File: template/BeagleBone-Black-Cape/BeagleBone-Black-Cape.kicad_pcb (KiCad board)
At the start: 2 copper layers, 54.6 x 86.4 mm, 2 parts, among them P8 BeagleBone_Black_Header, P9 BeagleBone_Black_Header

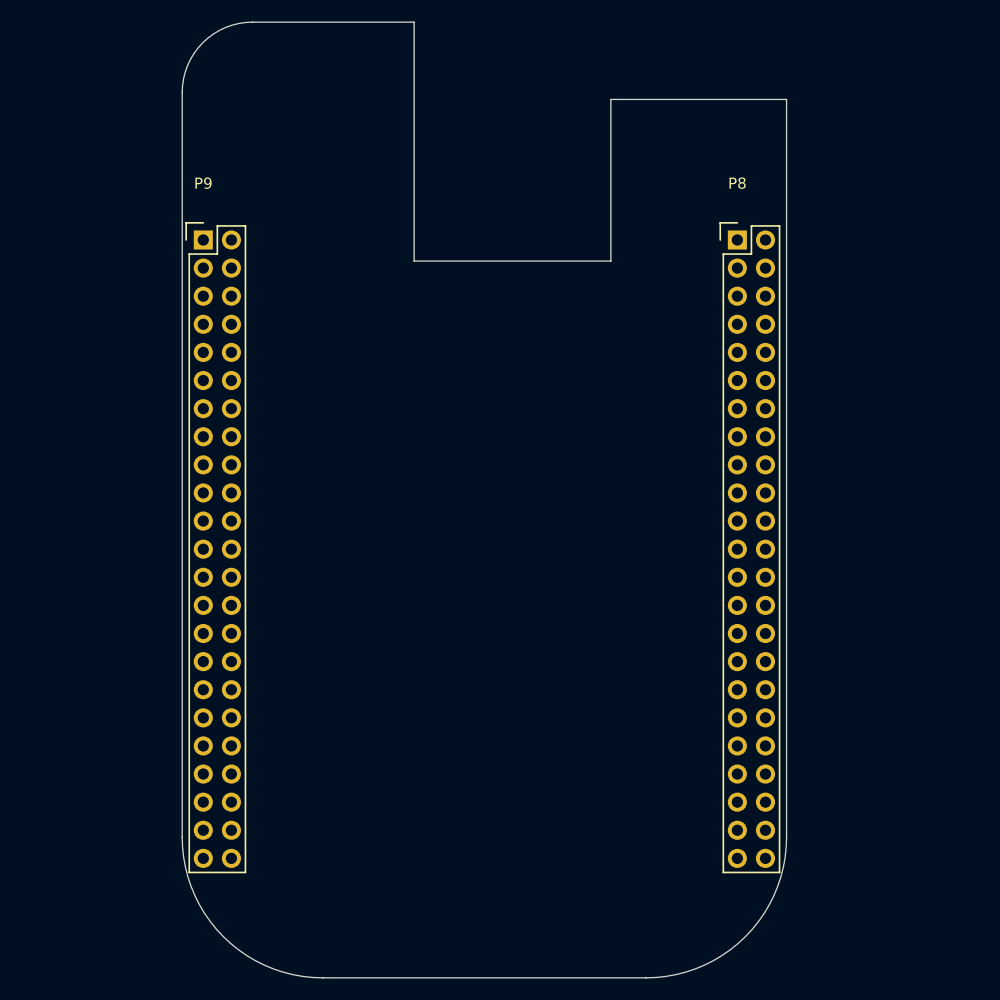
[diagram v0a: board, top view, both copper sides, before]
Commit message: fix: change original libs; add: new components
- Fix LIS3DH pins positions;
- Add ATmega164P symbol;
- Add 3D model to the L_Wuerth_HCM-7050;
- Add parameters for R_RES (Assembly...).
- Add parameters for R_RES and C_CAP;
- Fix SOIC-8 package 3D model;
- Add new parameters for many symbols;
- Change text height from 70 mil to 50 mil;
- Add solder mask expansion for 2-contact jumpers;
- Change thermopad vias of QFN-20-1EP_3x3mm_P0.45mm_EP1.6x1.6mm_ThermalVias;
- Add D_SMAF footprint;
- Fillet silk for C_1206;
-Rectangle silk for R_1206;
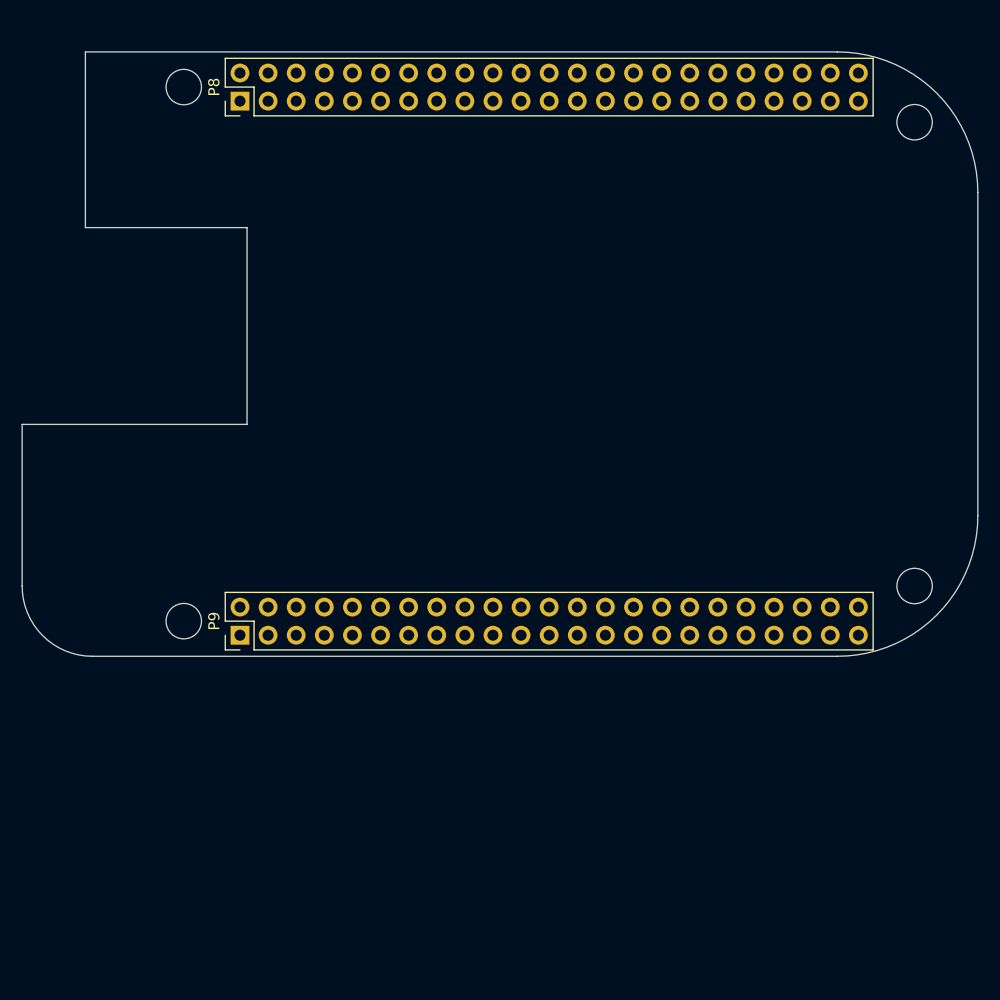
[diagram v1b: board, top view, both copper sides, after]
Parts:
- added MH1: MountingHole_3.2mm_M3_DIN965, MountingHole:MountingHole_3.2mm_M3_DIN965, F.Cu at (114.6, 48.6)
- added MH2: MountingHole_3.2mm_M3_DIN965, MountingHole:MountingHole_3.2mm_M3_DIN965, F.Cu at (114.6, 96.8)
- added MH3: MountingHole_3.2mm_M3_DIN965, MountingHole:MountingHole_3.2mm_M3_DIN965, F.Cu at (180.6, 51.7)
- added MH4: MountingHole_3.2mm_M3_DIN965, MountingHole:MountingHole_3.2mm_M3_DIN965, F.Cu at (180.6, 93.7)
- P8, P9: footprint Socket_BeagleBone_Black:Socket_BeagleBone_Black -> Connector_PinHeader_2.54mm:PinHeader_2x23_P2.54mm_Vertical
- moved P8 46.7 mm to (119.7, 49.8), turned to 90 degrees
- moved P9 35.9 mm to (119.7, 98.1), turned to 90 degrees
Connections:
- net GNDA_ADC renamed GNDA
- net Net-(P8-Pad10) renamed /GPIO[68]
- net Net-(P8-Pad11) renamed /GPIO[45]
- net Net-(P8-Pad12) renamed /GPIO[44]
- net Net-(P8-Pad13) renamed /GPIO[23]
- net Net-(P8-Pad14) renamed /GPIO[26]
- net Net-(P8-Pad15) renamed /GPIO[47]
- net Net-(P8-Pad16) renamed /GPIO[46]
- net Net-(P8-Pad17) renamed /GPIO[27]
- net Net-(P8-Pad18) renamed /GPIO[65]
- net Net-(P8-Pad19) renamed /GPIO[22]
- net Net-(P8-Pad20) renamed /MMC1.CMD
- net Net-(P8-Pad21) renamed /MMC1.CLK
- net Net-(P8-Pad22) renamed /MMC1.DAT[5]
- net Net-(P8-Pad23) renamed /MMC1.DAT[4]
- net Net-(P8-Pad24) renamed /MMC1.DAT[1]
- net Net-(P8-Pad25) renamed /MMC1.DAT[0]
- net Net-(P8-Pad26) renamed /LCD.PCLK
- net Net-(P8-Pad27) renamed /LCD.VSYNC
- net Net-(P8-Pad28) renamed /GPIO[61]
- net Net-(P8-Pad29) renamed /LCD.HSYNC
- net Net-(P8-Pad3) renamed /MMC1.DAT[6]
- net Net-(P8-Pad30) renamed /LCD.AC_BIAS_E
- net Net-(P8-Pad31) renamed /LCD.DATA[14]
- net Net-(P8-Pad32) renamed /LCD.DATA[15]
- net Net-(P8-Pad33) renamed /LCD.DATA[13]
- net Net-(P8-Pad34) renamed /LCD.DATA[11]
- net Net-(P8-Pad35) renamed /LCD.DATA[8]
- net Net-(P8-Pad36) renamed /LCD.DATA[10]
- net Net-(P8-Pad37) renamed /LCD.DATA[6]
- net Net-(P8-Pad38) renamed /LCD.DATA[9]
- net Net-(P8-Pad39) renamed /LCD.DATA[4]
- net Net-(P8-Pad4) renamed /MMC1.DAT[7]
- net Net-(P8-Pad40) renamed /LCD.DATA[7]
- net Net-(P8-Pad41) renamed /LCD.DATA[2]
- net Net-(P8-Pad42) renamed /LCD.DATA[5]
- net Net-(P8-Pad43) renamed /LCD.DATA[0]
- net Net-(P8-Pad44) renamed /LCD.DATA[3]
- net Net-(P8-Pad46) renamed /LCD.DATA[1]
- net Net-(P8-Pad5) renamed /MMC1.DAT[2]
- net Net-(P8-Pad6) renamed /MMC1.DAT[3]
- net Net-(P8-Pad7) renamed /GPIO[66]
- net Net-(P8-Pad8) renamed /GPIO[67]
- net Net-(P8-Pad9) renamed /GPIO[69]
- net Net-(P9-Pad11) renamed /GPIO[30]
- net Net-(P9-Pad12) renamed /GPIO[60]
- net Net-(P9-Pad13) renamed /GPIO[31]
- net Net-(P9-Pad14) renamed /GPIO[40]
- net Net-(P9-Pad15) renamed /GPIO[48]
- net Net-(P9-Pad16) renamed /GPIO[51]
- net Net-(P9-Pad17) renamed /GPIO[4]
- net Net-(P9-Pad18) renamed /GPIO[5]
- net Net-(P9-Pad19) renamed /I2C2.SCL
- net Net-(P9-Pad20) renamed /I2C2.SDA
- net Net-(P9-Pad21) renamed /GPIO[3]
- net Net-(P9-Pad22) renamed /GPIO[2]
- net Net-(P9-Pad23) renamed /GPIO[49]
- net Net-(P9-Pad24) renamed /GPIO[15]
- net Net-(P9-Pad25) renamed /GPIO[117]
- net Net-(P9-Pad26) renamed /GPIO[14]
- net Net-(P9-Pad27) renamed /GPIO[125]
- net Net-(P9-Pad28) renamed /SPI1.CS0
- net Net-(P9-Pad29) renamed /SPI1.D0
- net Net-(P9-Pad30) renamed /GPIO[122]
- net Net-(P9-Pad31) renamed /SPI1.SCLK
- net Net-(P9-Pad33) renamed /AIN4
- net Net-(P9-Pad35) renamed /AIN6
- net Net-(P9-Pad36) renamed /AIN5
- net Net-(P9-Pad37) renamed /AIN2
- net Net-(P9-Pad38) renamed /AIN3
- net Net-(P9-Pad39) renamed /AIN0
- net Net-(P9-Pad40) renamed /AIN1
- net Net-(P9-Pad41) renamed /GPIO[20]
- net Net-(P9-Pad42) renamed /GPIO[7]
- net PWR_BUT renamed /PWR_BUT
- net SYS_5V renamed VBUS
- net SYS_RESETN renamed /~{SYS_RESET}
- net VDD_ADC renamed +1V8
- P8 pad 45: Net-(P8-Pad45) -> GNDD
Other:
- board size 54.6 x 86.4 mm -> 86.4 x 54.6 mm
- board text added: "Note: due to to way pin numbers work on the BBB, the connectors are actually 2.54mm pin headers with the 3D models overridden."
